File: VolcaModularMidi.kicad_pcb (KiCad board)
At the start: 2 copper layers, 30 x 18.2 mm, 6 parts, among them J1 Conn_01x04_Male, J2 MIDI_IN, U1 6N139

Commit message: Finished routing and laying out pcb
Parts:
- J1: value Conn_01x04_Male -> Conn_01x03_Female; footprint Connector_PinHeader_2.54mm:PinHeader_1x04_P2.54mm_Vertical -> Connector_PinSocket_2.00mm:PinSocket_1x03_P2.00mm_Vertical
- J2: value MIDI_IN -> (none); footprint SensaiLib:din-5 -> eurocad:MIDI_DIN5
- R1, R2: moved to F.Cu
- U1: value 6N139 -> 6N137; footprint Package_DIP:DIP-8_W7.62mm -> Package_DIP:DIP-8_W7.62mm_LongPads
- moved J2 68.6 mm to (86.4, 71.1), turned to -90 degrees
- moved R1 50.6 mm to (108.0, 76.2), turned to 180 degrees
- moved U1 49.1 mm to (114.3, 64.8)
- moved J1 48.8 mm to (137.2, 66.6)
- moved R2 48.1 mm to (129.5, 64.8), turned to -90 degrees
- moved D1 46.1 mm to (108.0, 66.0), turned to 180 degrees
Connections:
- J1 pad 1: RX -> VCC
- J1 pad 2: TX -> RX
- J1 pad 3: VCC -> GND
- J2 pad 1: Net-(J2-Pad1) -> unconnected-(J2-Pad1)
- J2 pad 2: Net-(J2-Pad2) -> unconnected-(J2-Pad2)
- J2 pad 3: Net-(J2-Pad3) -> unconnected-(J2-Pad3)
- U1 pad 1: Net-(U1-Pad1) -> unconnected-(U1-Pad1)
- U1 pad 4: Net-(U1-Pad4) -> unconnected-(U1-Pad4)
- U1 pad 7: Net-(U1-Pad7) -> unconnected-(U1-Pad7)
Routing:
- net GND: track 0.00 -> 16.0 mm
- net RX: track 31.3 -> 17.9 mm, vias 1 -> 0
- net Net-(J2-Pad4): track 13.6 -> 8.51 mm
- net Net-(D1-Pad1): track 21.8 -> 17.0 mm, vias 1 -> 0
- net VCC: track 20.6 -> 16.0 mm
- net Net-(D1-Pad2): track 23.3 -> 24.1 mm
- removed copper zone on B.Cu, net GND
- removed copper zone on F.Cu, net GND
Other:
- board size 30 x 18.2 mm -> 64.8 x 22.9 mm
- net class Default removed
- rule pad_to_mask_clearance: 0.051 -> 0
- board text added: "Volca Modular MIDI IN (^_^)"
- board text removed: "+"
- board text removed: "-"
- board text removed: "R"
- board text removed: "T"
- board text removed: "Volca Modular Midi V0.1"
- board text removed: "github.com/sensai7"

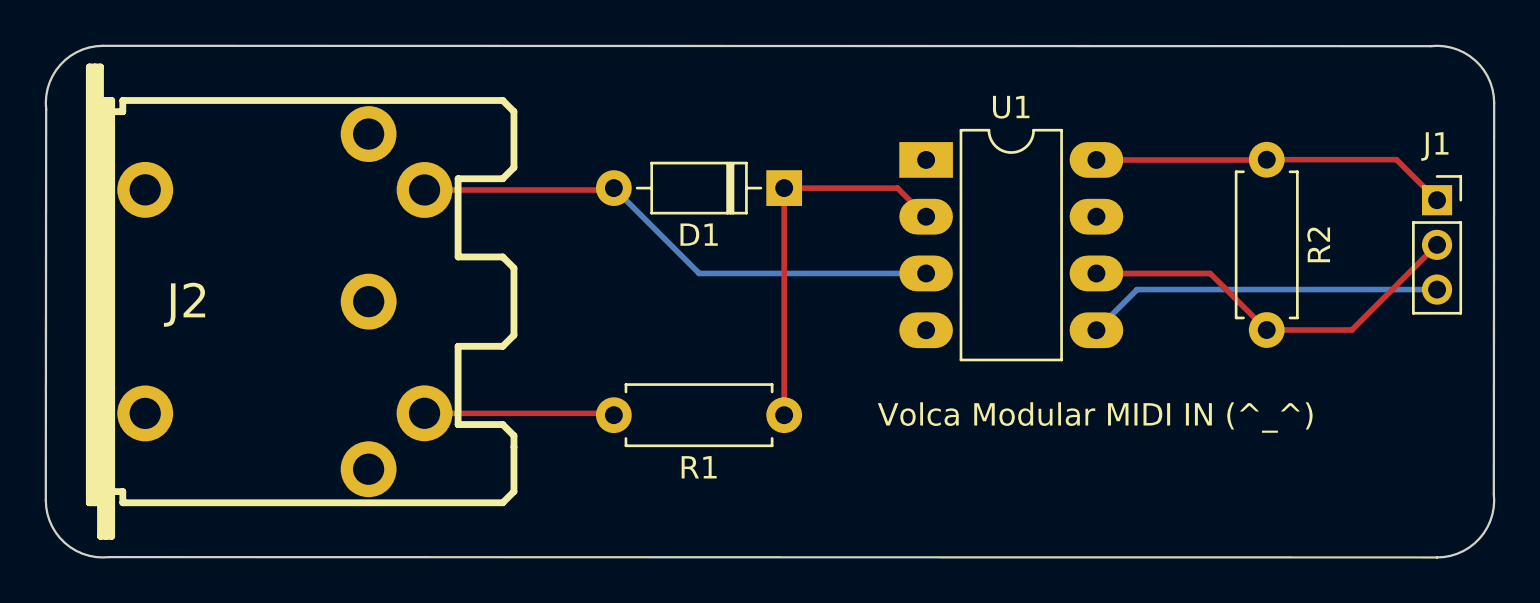
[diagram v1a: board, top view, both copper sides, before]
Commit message: Added mounting holes, replaced jumper connector with jst connector
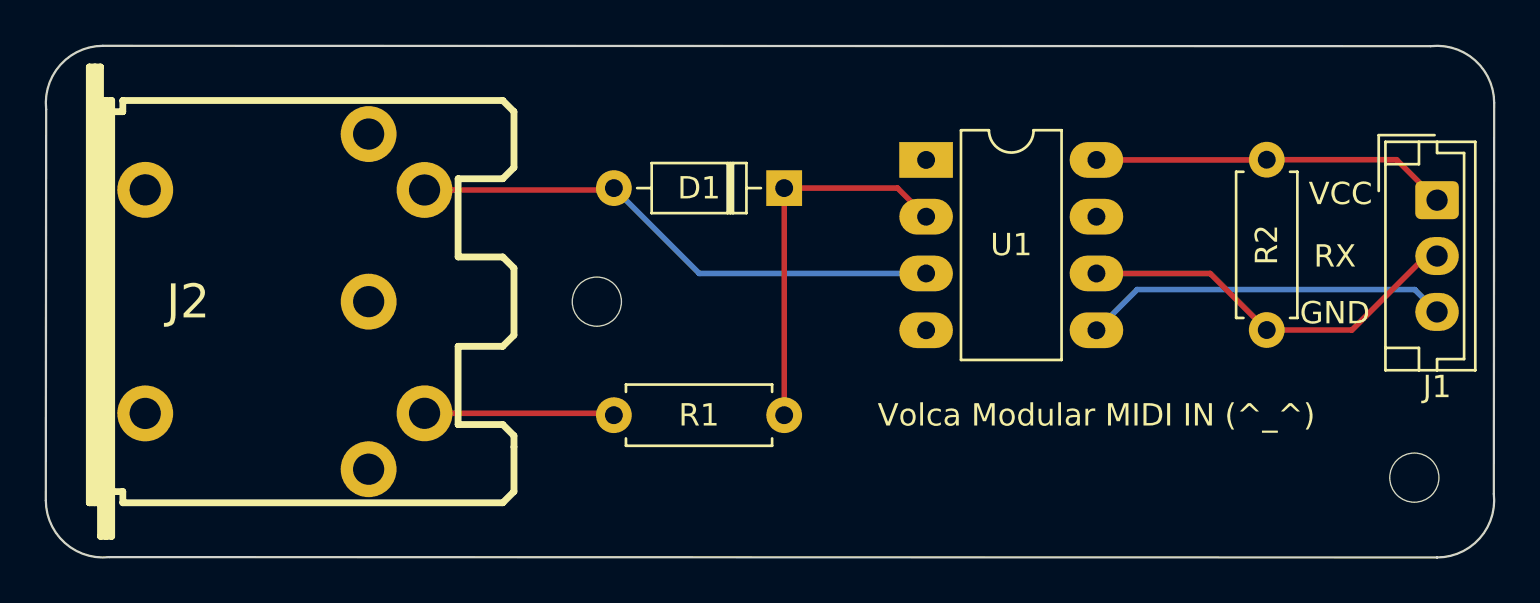
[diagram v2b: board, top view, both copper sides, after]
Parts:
- added REF**: MountingHole_2.2mm_M2, MountingHole:MountingHole_2.2mm_M2, F.Cu at (136.1, 79.0)
- added REF**: MountingHole_2.2mm_M2, MountingHole:MountingHole_2.2mm_M2, F.Cu at (99.6, 71.1)
- J1: footprint Connector_PinSocket_2.00mm:PinSocket_1x03_P2.00mm_Vertical -> Connector_JST:JST_EH_B3B-EH-A_1x03_P2.50mm_Vertical
- J2: value (none) -> MIDI_IN
- turned J1 to -90 degrees
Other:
- board text added: "GND"
- board text added: "RX"
- board text added: "VCC"

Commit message: Added URL QR code
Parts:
- added  : , VolcaMidiUrl:volcaMidiProjUrl, B.Cu at (120.4, 78.5)
- added  : OSHW-Logo2_7.3x6mm_SilkScreen, Symbol:OSHW-Logo2_7.3x6mm_SilkScreen, B.Cu at (113.3, 78.5)
